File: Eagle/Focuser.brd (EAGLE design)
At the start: 97.8 x 46.7 mm, 28 parts, among them IC1 L7805, IC2 L7805, Q1 IRF540, Q2 IRF540, Q3 IRF540

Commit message: Circuit for commercial version
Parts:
- removed 12V-OUT, JP1: (no value), pinhead:1X02
- removed C1, C2: 10uF, rcl:C025-024X044
- removed D1: (no value), diode:D-2.5
- removed FUSE2: 2A, fuse:FUSE_HOLDER_5X20MM
- removed IC1, IC2: L7805, linear:TO220V
- removed JP3, JP4, JP5: (no value), SparkFun-Connectors:SCREWTERMINAL-5MM-2
- removed Q1, Q2, Q3: IRF540, transistor-power:TO220BV
- removed R2, R3, R4: 4.7K, rcl:0204/5
- removed R5: (no value), pot:B64Y
- removed R6: 220R, resistor:0204/5
- removed USB1: FEMALE A, Seeed-Connector:USB4+2P-2.0-90D
- FUSE1: value 1.5A -> 1A
- moved FUSE1 75.2 mm to (39.4, 34.3), turned to 180 degrees
- moved VIN 64.8 mm to (33.0, 43.2)
- moved U$1 30.2 mm to (7.62, 30.5)
- moved R1 29.9 mm to (24.1, 3.81)
- moved C3 28.7 mm to (29.2, 25.4)
- moved LED1 28.7 mm to (30.5, 2.54)
- moved DRV1 27.4 mm to (21.6, 27.9)
- moved JP2 27.1 mm to (40.5, 17.8)
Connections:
- removed net D3: Q3.G, R2.2, U$1.D3
- removed net D5: Q2.G, R4.2, U$1.D5
- removed net D6: Q1.G, R3.2, U$1.D6
- removed net N$10: JP4.2, Q1.D
- removed net N$11: JP5.2, Q3.D
- removed net N$19: JP1.1, R6.1
- removed net N$2: R5.S, U$1.A7
- removed net N$3: R6.2, U$1.D11
- removed net N$4: C1.1, FUSE1.2, IC1.1, IC2.1
- removed net N$8: 12V-OUT.2, FUSE1.1, FUSE2.1, VIN.2
- removed net N$9: D1.A, JP3.2, Q2.D
- new net N$7: FUSE1.1, VIN.2
- net +12V: now also FUSE1.2, U$1.RAW; no longer D1.C, FUSE2.2, JP3.1, JP4.1, JP5.1
- net +5V: no longer C2.1, IC1.3, IC2.3, R5.A, USB1.1
- net GND: no longer 12V-OUT.1, C1.2, C2.2, IC1.2, IC2.2, JP1.2, Q1.S, Q2.S, Q3.S, R2.1, R3.1, R4.1, R5.E, U$1.GND1, USB1.4
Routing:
- net GND: track 251.4 -> 79.4 mm, vias 1 -> 0
- net +12V: track 158.6 -> 30.0 mm
- net +5V: track 118.0 -> 24.8 mm
- net N$4: track 39.2 -> 0.00 mm
- net N$8: track 26.7 -> 0.00 mm
- net N$9: track 25.8 -> 0.00 mm
- net N$11: track 21.9 -> 0.00 mm
- net D6: track 21.1 -> 0.00 mm
- net N$7: track 0.00 -> 20.4 mm
- net D3: track 20.1 -> 0.00 mm
- net D5: track 14.1 -> 0.00 mm
- net N$2: track 12.3 -> 0.00 mm
- net N$10: track 9.45 -> 0.00 mm
- net N$3: track 3.81 -> 0.00 mm
- net N$18: track 8.73 -> 6.13 mm
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- removed copper zone on layer 1, net GND
- removed copper zone on layer 16, net GND
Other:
- board size 97.8 x 46.7 mm -> 43.2 x 46.7 mm
- board text removed: "Arduino Nano"

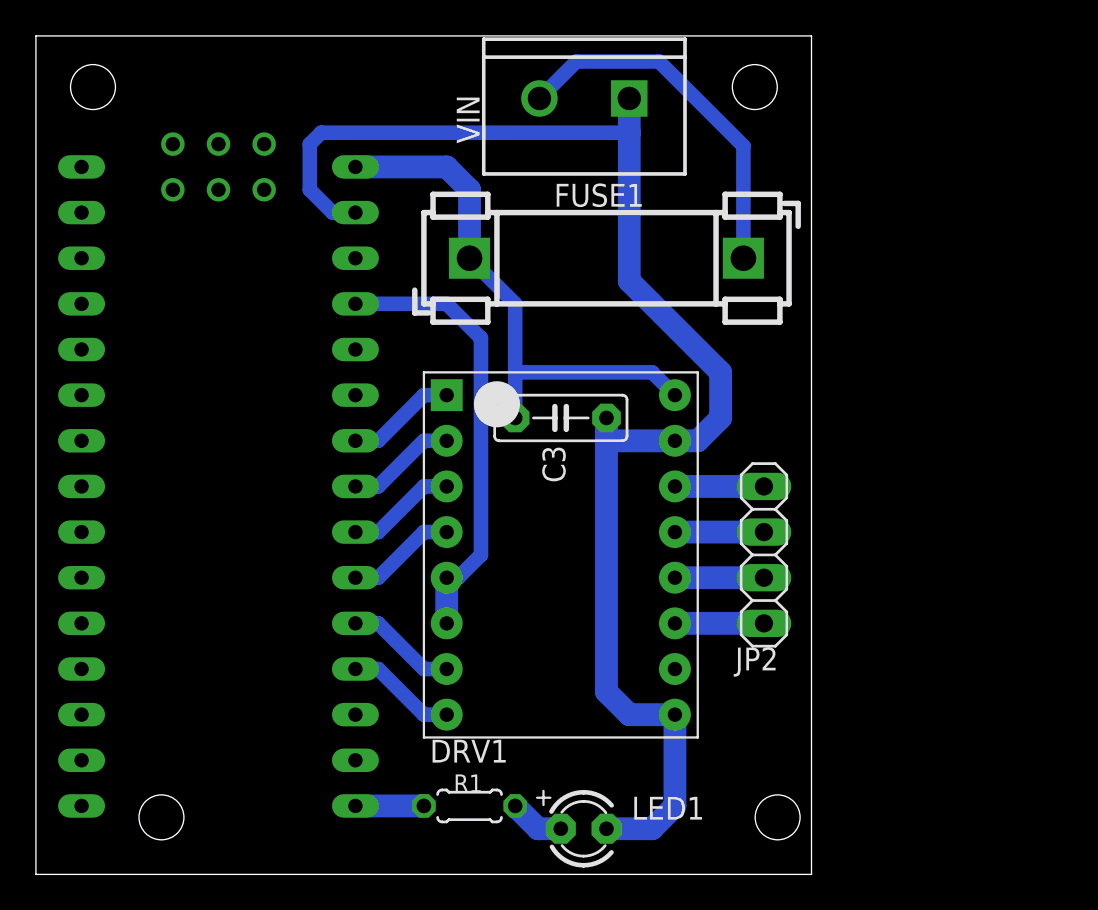
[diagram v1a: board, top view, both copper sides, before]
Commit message: Hand control added in circuit
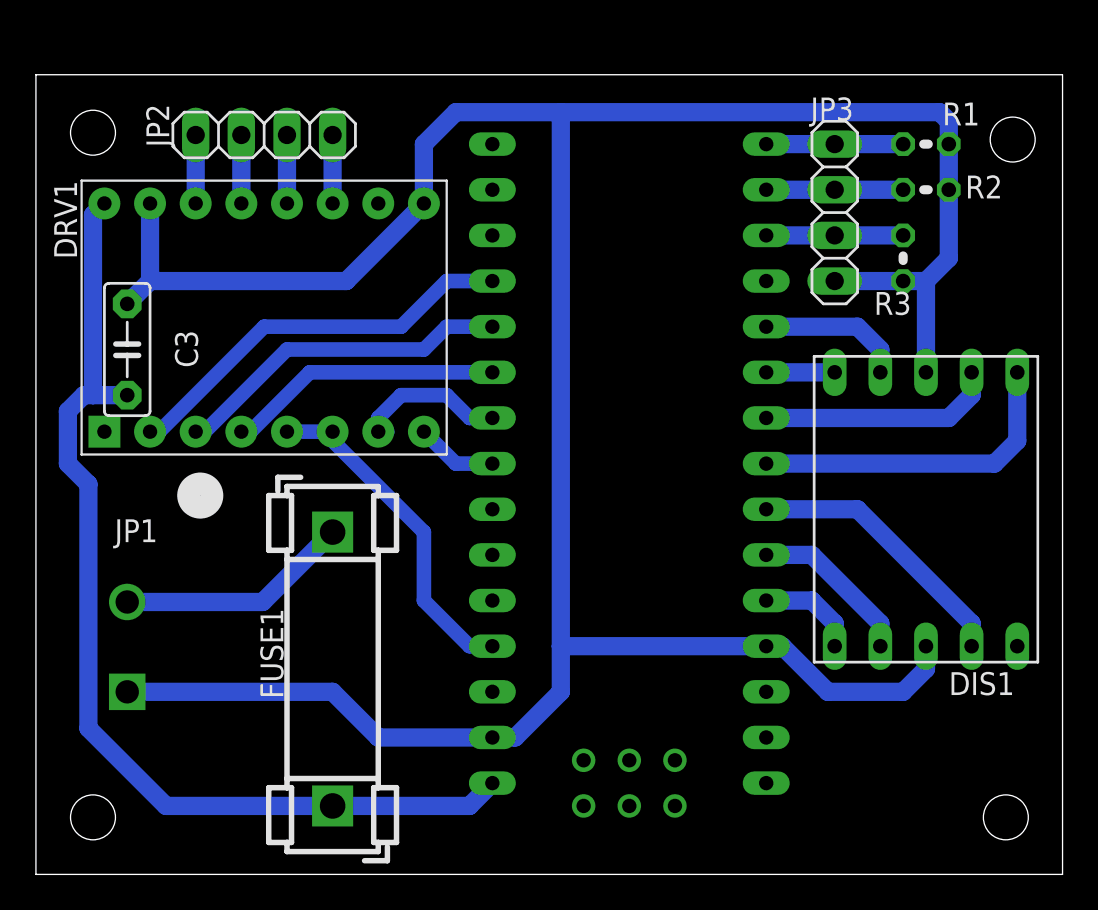
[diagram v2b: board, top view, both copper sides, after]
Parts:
- removed LED1: RED, adafruit:LED3MM
- removed VIN: (no value), SparkFun-Connectors:SCREWTERMINAL-5MM-2
- added DIS1: HD-H101, display-hp:HDSP-M
- added JP1: (no value), SparkFun-Connectors:SCREWTERMINAL-5MM-2
- added JP3: BUTTONS, pinhead:1X04
- added R2, R3: 10K, resistor:0204V
- R1: value 220R -> 10K; device resistor:0204/5 -> resistor:0204V
- moved R1 44.7 mm to (49.5, 40.6), turned to 0 degrees
- moved JP2 36.3 mm to (12.7, 41.1), turned to 0 degrees
- moved U$1 32.5 mm to (35.6, 14.0), turned to 0 degrees
- moved FUSE1 27.5 mm to (16.5, 19.1), turned to 270 degrees
- moved C3 24.4 mm to (5.08, 29.2), turned to 270 degrees
- moved DRV1 19.6 mm to (2.54, 23.4), turned to 90 degrees
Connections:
- removed net D13: R1.2, U$1.D13
- new net N$10: DIS1.7, U$1.D6
- new net N$11: DIS1.10, U$1.D7
- new net N$19: DIS1.9, U$1.D8
- new net N$2: JP3.3, R3.1, U$1.D10
- new net N$3: JP3.2, R2.1, U$1.D11
- new net N$4: JP3.1, R1.1, U$1.D12
- new net N$8: DIS1.4, U$1.D4
- new net N$9: DIS1.6, U$1.D5
- net GND: now also DIS1.3, DIS1.8, JP1.1, JP3.4, R1.2, R2.2, R3.2, U$1.GND1; no longer LED1.K, VIN.1
- net N$1: now also DIS1.1, U$1.D2; no longer LED1.A, R1.1
- net N$12: now also U$1.A3; no longer U$1.A1
- net N$18: now also U$1.A1; no longer U$1.A3
- net N$20: now also U$1.A0; no longer U$1.A4
- net N$5: now also U$1.A4; no longer U$1.A0
- net N$6: now also DIS1.2, U$1.D3; no longer DRV1.ENABLE, U$1.A5
- net N$7: now also JP1.2; no longer VIN.2
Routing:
- net GND: track 79.4 -> 157.8 mm
- net +12V: track 30.0 -> 57.5 mm
- net N$9: track 0.00 -> 18.3 mm
- net N$20: track 6.13 -> 22.5 mm
- net N$8: track 0.00 -> 15.3 mm
- net N$10: track 0.00 -> 13.2 mm
- net N$18: track 6.13 -> 18.9 mm
- net N$17: track 6.13 -> 15.3 mm
- net N$19: track 0.00 -> 8.15 mm
- net N$4: track 0.00 -> 7.62 mm
- net N$3: track 0.00 -> 7.62 mm
- net N$2: track 0.00 -> 7.62 mm
- net N$7: track 20.4 -> 13.0 mm
- net +5V: track 24.8 -> 18.9 mm
- net N$11: track 0.00 -> 3.81 mm
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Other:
- board size 43.2 x 46.7 mm -> 57.1 x 44.5 mm
